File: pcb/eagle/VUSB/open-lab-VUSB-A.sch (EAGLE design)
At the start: 68 parts, among them IC1 ATMEGA328P, IC2 MCP73831, IC4 MCP1700-33, IC6 MAX31855, IC7 ENC28J60, J1 AYZ0202, Q2 BSS123, U3 BMP085, X1 USBSMD, X2 32.768kHz, X3 25MHz

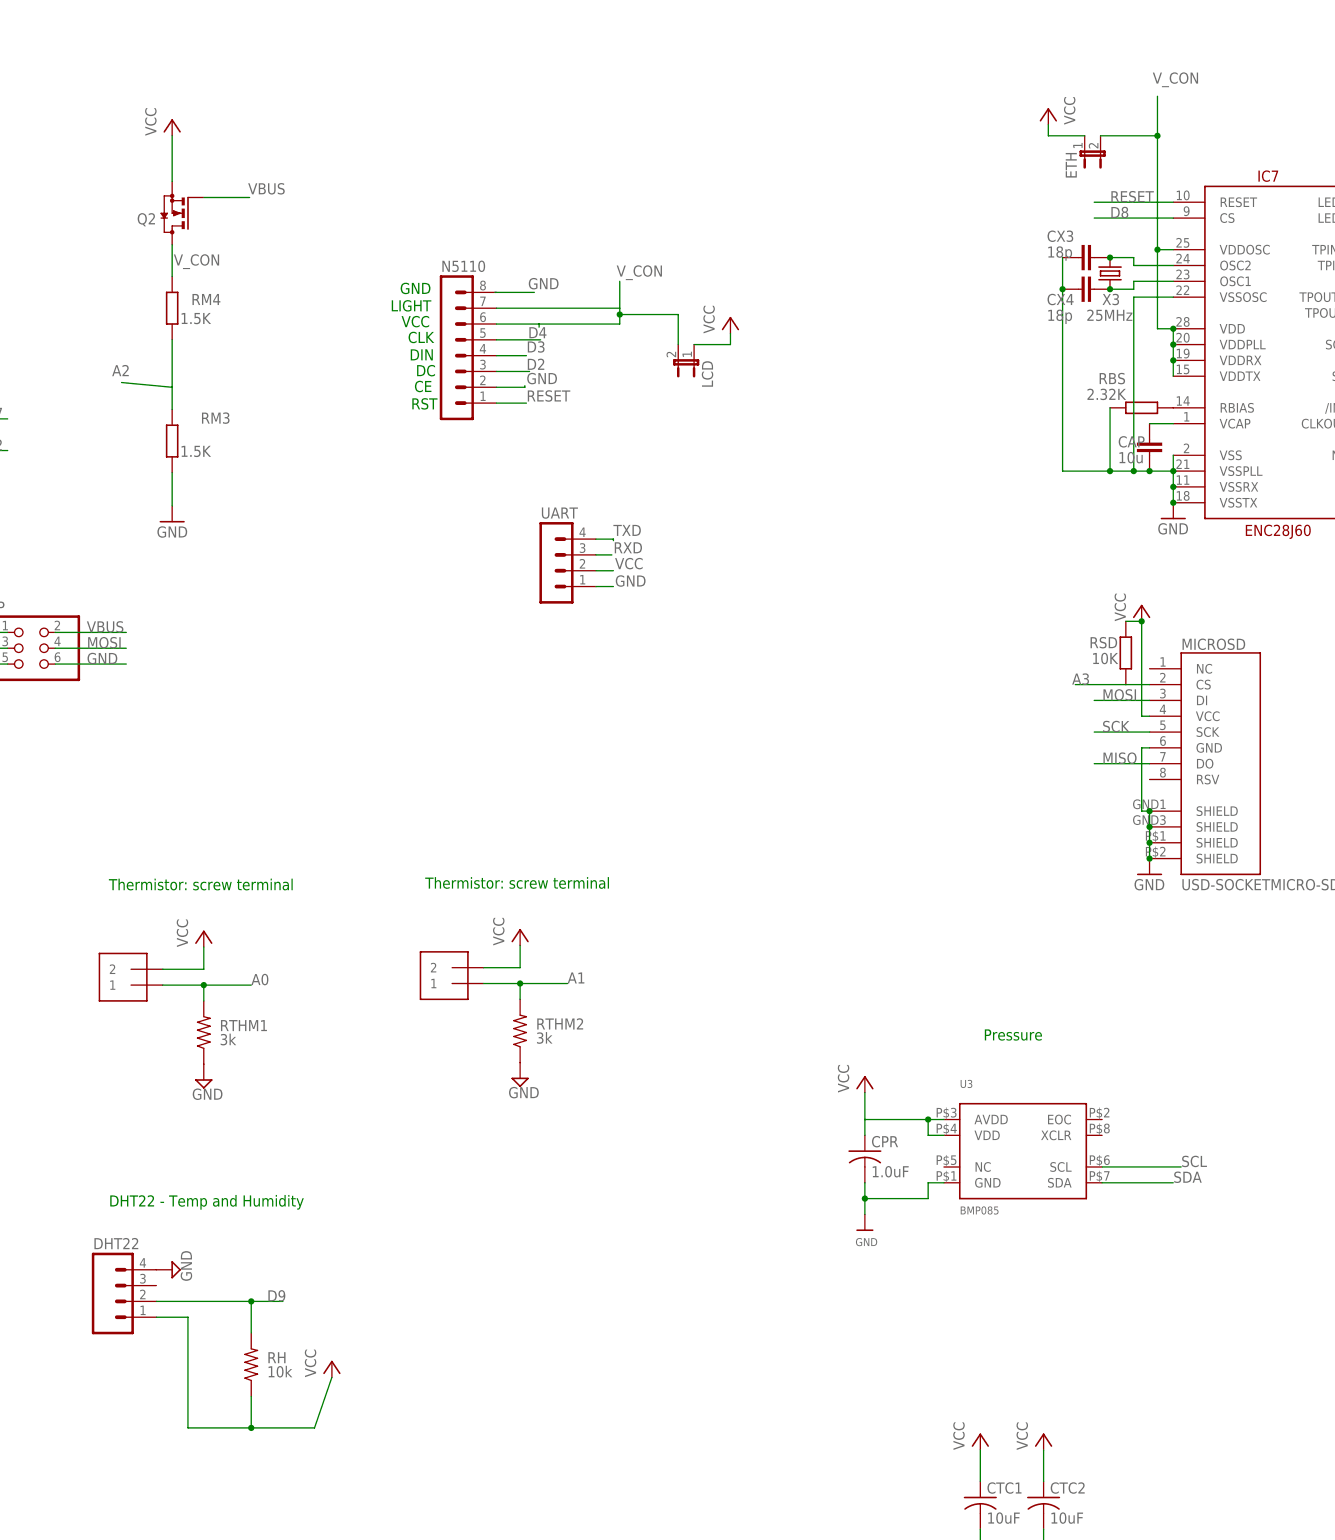
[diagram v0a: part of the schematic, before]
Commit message: fixed some pin assignments
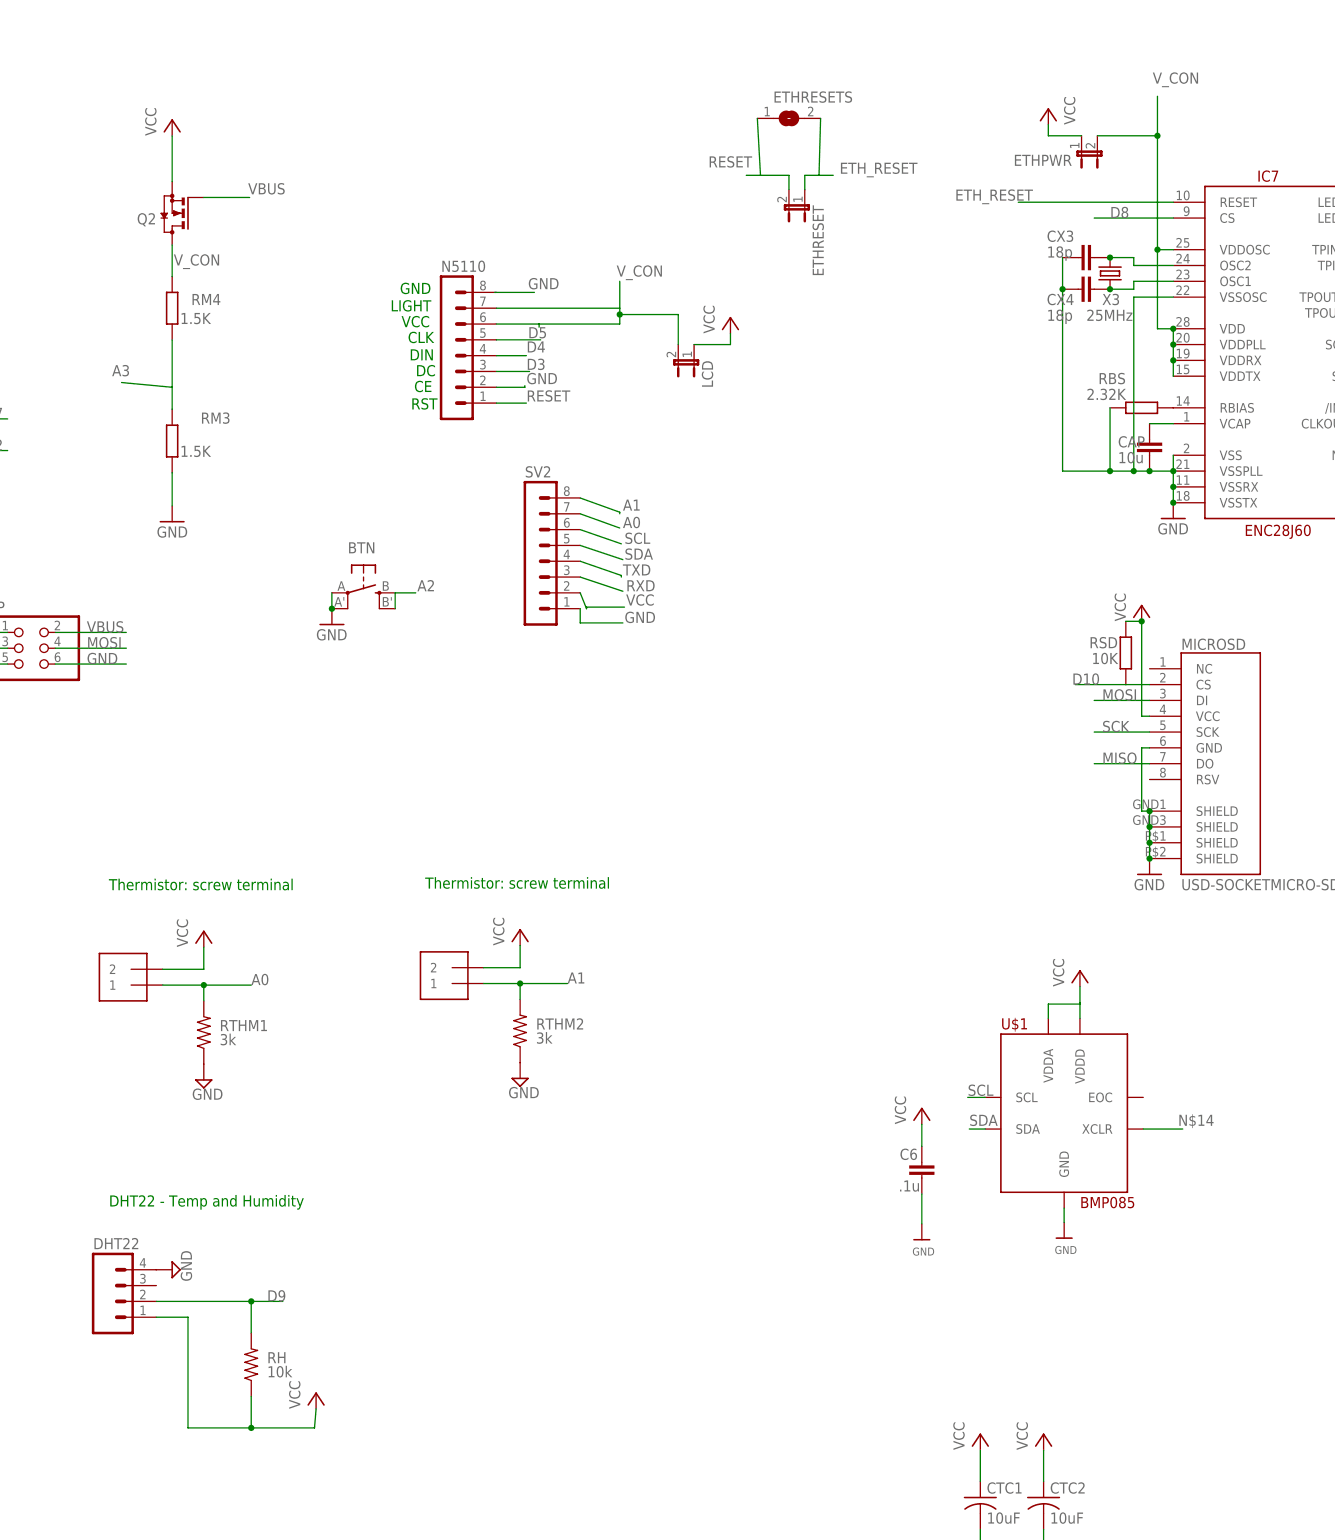
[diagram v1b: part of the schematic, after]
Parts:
- removed CPR: 1.0uF, adafruit:C-USC0805
- removed ETH: (no value), jumper:JP1E
- removed U3: BMP085, microbuilder:BMP085
- removed UART: (no value), con-lstb:MA04-1
- added BTN: EVQQ2, adafruit:EVQQ2
- added C6: .1u, resistor:C-EUC0805
- added ETHPWR, ETHRESET: (no value), jumper:JP1E
- added ETHRESETS: (no value), jumper:SJ
- added SV2: (no value), con-lstb:MA08-1
- added U$1: BMP085, JeeLabs:BMP085
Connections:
- new net ETH_RESET: ETHRESET.1, ETHRESETS.2, IC7.RESET
- new net N$14: U$1.XCLR
- net A0: now also SV2.7
- net A1: now also SV2.8
- net A2: now also BTN.S, BTN.S1; no longer RM3.2, RM4.1
- net A3: now also RM3.2, RM4.1; no longer MICROSD.CS, RSD.1
- net D10: now also MICROSD.CS, RSD.1
- net D2: no longer N5110.3
- net D3: now also N5110.3; no longer N5110.4
- net D4: now also N5110.4; no longer N5110.5
- net D5: now also N5110.5
- net GND: now also BTN.P, BTN.P1, C6.2, SV2.1, U$1.GND; no longer CPR.2, U3.GND, UART.1
- net RESET: now also ETHRESET.2, ETHRESETS.1; no longer IC7.RESET
- net RXD: now also SV2.3; no longer UART.3
- net SCL: now also SV2.6, U$1.SCL; no longer U3.SCL
- net SDA: now also SV2.5, U$1.SDA; no longer U3.SDA
- net TXD: now also SV2.4; no longer UART.4
- net VCC: now also C6.1, ETHPWR.1, SV2.2, U$1.VDDA, U$1.VDDD; no longer CPR.1, ETH.1, U3.AVDD, U3.VDD, UART.2
- net V_CON: now also ETHPWR.2; no longer ETH.2
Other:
- note removed: "Pressure"

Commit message: update
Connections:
- removed net N$14: U$1.XCLR
- net VCC: now also U$1.XCLR
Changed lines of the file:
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@@
 <part name="P+18" library="supply1" deviceset="VCC" device=""/>
 <part name="C6" library="resistor" deviceset="C-EU" device="C0805" value=".1u"/>
+<part name="P+17" library="supply1" deviceset="VCC" device=""/>
 </parts>
 <sheets>
@@
 <attribute name="VALUE" x="265.938" y="-11.811" size="1.778" layer="96" rot="R180"/>
 </instance>
+<instance part="P+17" gate="VCC" x="308.102" y="4.572"/>
 </instances>
 <busses>
@@
 <pinref part="C6" gate="G$1" pin="1"/>
 </segment>
+<segment>
+<pinref part="U$1" gate="G$1" pin="XCLR"/>
+<wire x1="301.752" y1="-3.556" x2="308.102" y2="-3.556" width="0.1524" layer="91"/>
+<label x="307.34" y="-3.048" size="1.778" layer="95"/>
+<wire x1="308.102" y1="-3.556" x2="308.102" y2="2.032" width="0.1524" layer="91"/>
+<pinref part="P+17" gate="VCC" pin="VCC"/>
+</segment>
 </net>
 <net name="AREF" class="0">
@@
 </segment>
 </net>
-<net name="N$14" class="0">
-<segment>
-<pinref part="U$1" gate="G$1" pin="XCLR"/>
-<wire x1="301.752" y1="-3.556" x2="308.102" y2="-3.556" width="0.1524" layer="91"/>
-<label x="307.34" y="-3.048" size="1.778" layer="95"/>
-</segment>
-</net>
